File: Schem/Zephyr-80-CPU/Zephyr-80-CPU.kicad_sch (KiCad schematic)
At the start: 0 parts

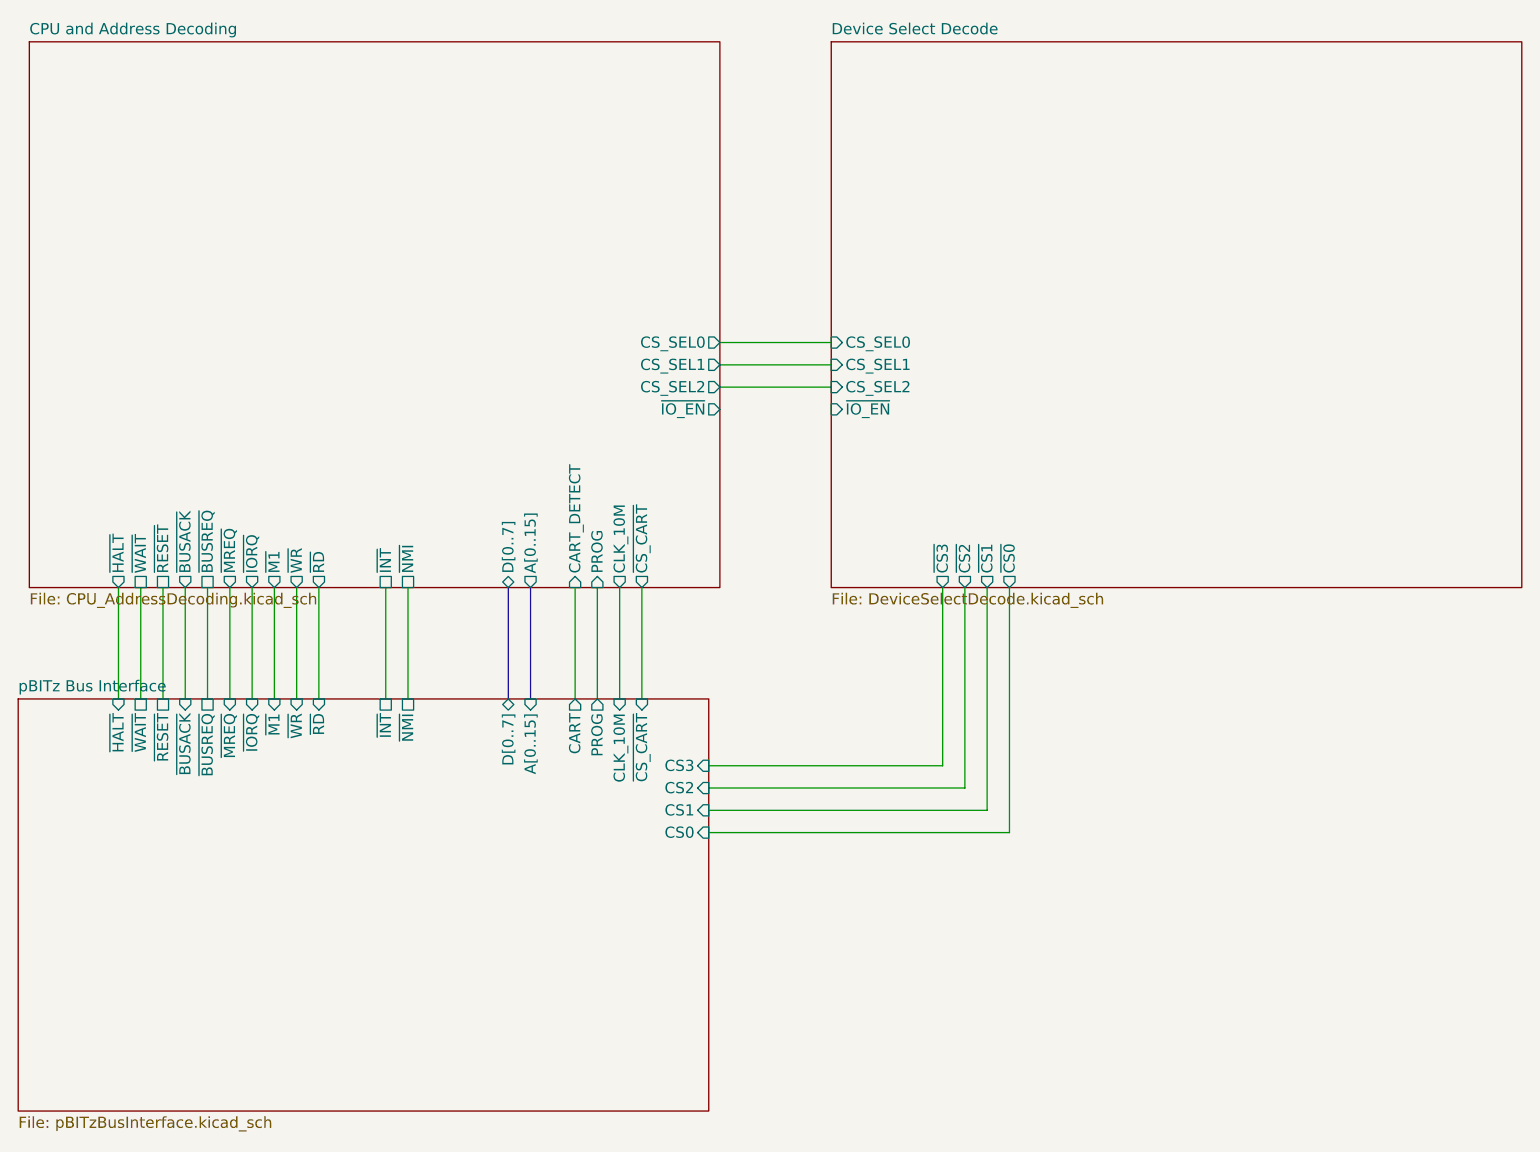
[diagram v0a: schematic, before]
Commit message: Routed the CPU board. Removed the rotary switches decoder
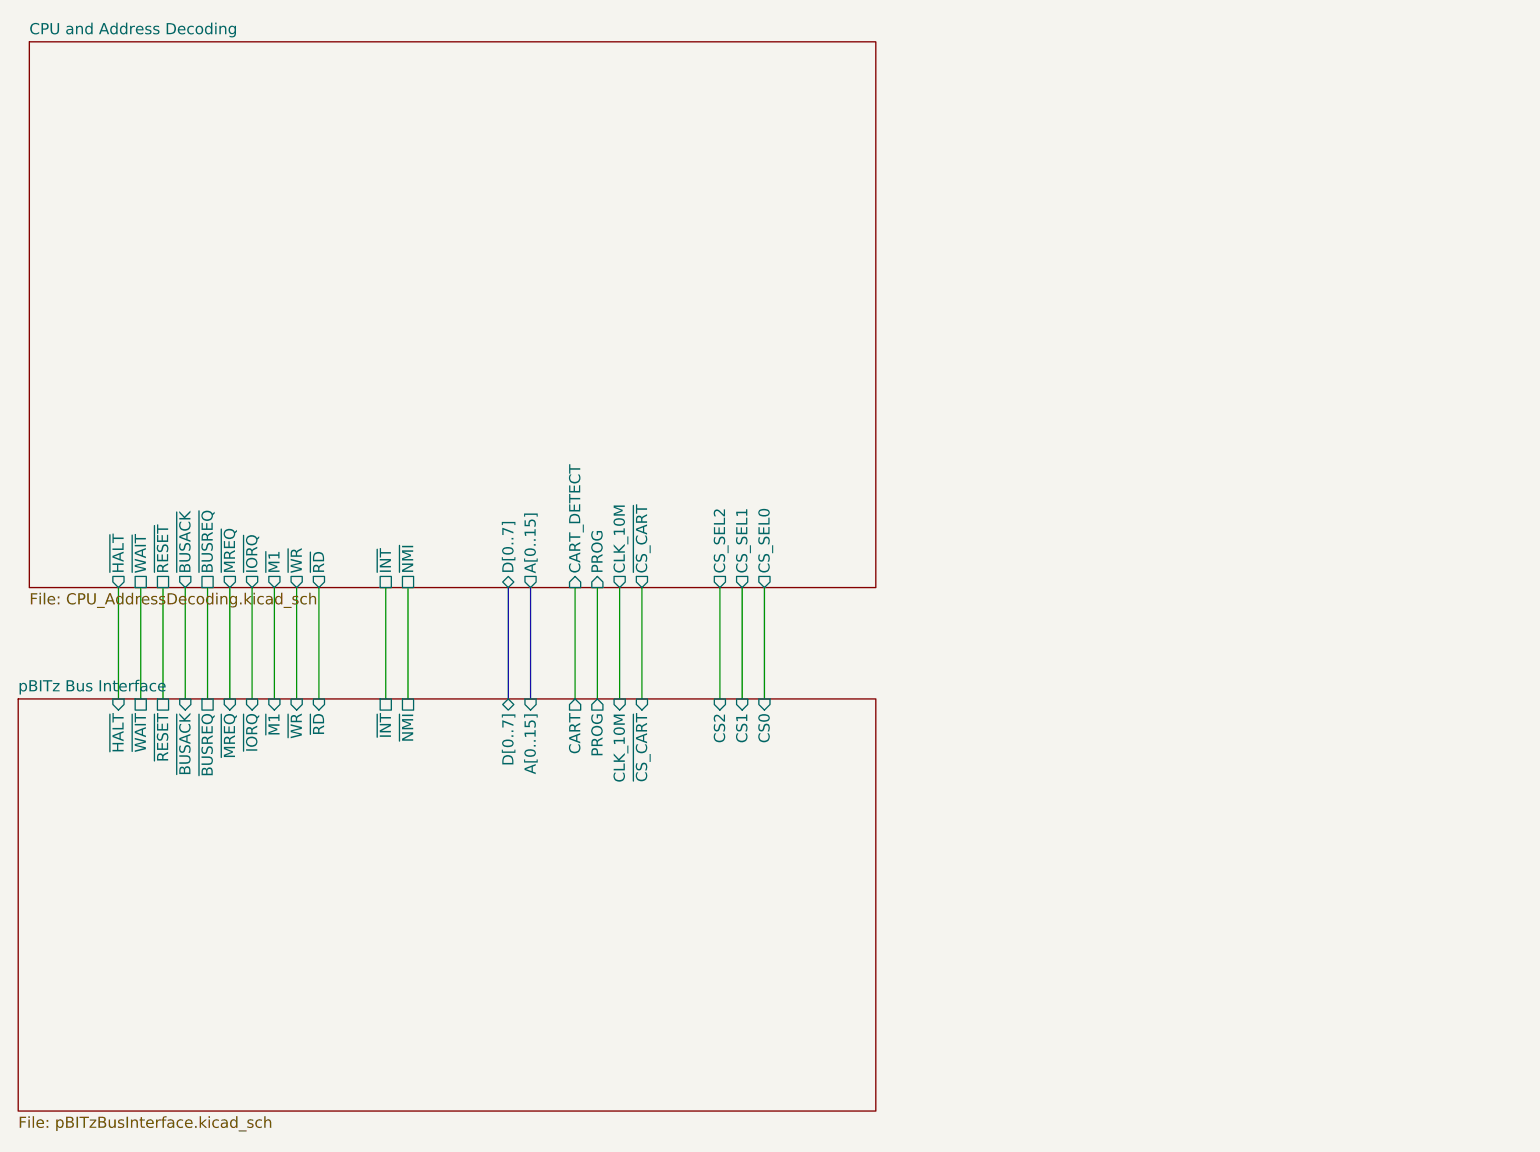
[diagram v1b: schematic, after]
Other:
- removed sheet Device Select Decode
- sheet CPU and Address Decoding ports: added none; removed ~{IO_EN}
- sheet pBITz Bus Interface ports: added none; removed CS3

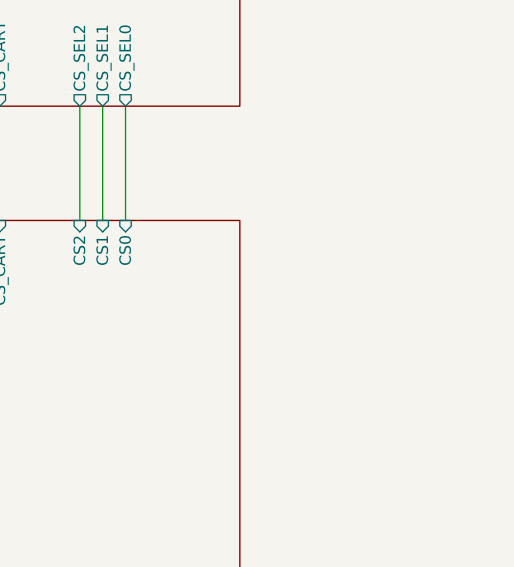
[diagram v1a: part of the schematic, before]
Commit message: Added all the manufacturer part numbers to the KiCad schematics and PCB files. This will make it easier to order the parts for the project and ensure that the correct components are used. I also removed some of the old schematics that were no longer needed, such as the BaudClock, ConsolePort, DeviceSelectDecode, GPIOUserSerial, IO Controller, UserPorts, Video, and Z80HomeBrew schematics. These changes will help to streamline the design and make it easier to understand.
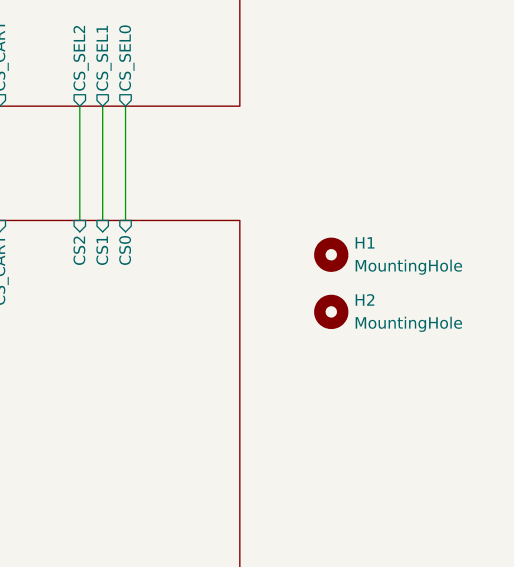
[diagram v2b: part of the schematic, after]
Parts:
- added H1, H2: MountingHole, MountingHole:MountingHole_2.2mm_M2, symbol Mechanical:MountingHole
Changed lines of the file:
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@@
+		)
+	)
+	(symbol
+		(lib_id "Mechanical:MountingHole")
+		(at 134.62 119.38 0)
+		(unit 1)
+		(exclude_from_sim no)
+		(in_bom no)
+		(on_board yes)
+		(dnp no)
+		(fields_autoplaced yes)
+		(property "Reference" "H2"
+			(at 137.16 118.1099 0)
+			(effects
+				(font
+					(size 1.27 1.27)
+				)
+				(justify left)
+			)
+		)
+		(property "Value" "MountingHole"
+			(at 137.16 120.6499 0)
+			(effects
+				(font
+					(size 1.27 1.27)
+				)
+				(justify left)
+			)
+		)
+		(property "Footprint" "MountingHole:MountingHole_2.2mm_M2"
+			(at 134.62 119.38 0)
+			(effects
+				(font
+					(size 1.27 1.27)
+				)
+				(hide yes)
+			)
+		)
+		(property "Datasheet" "~"
+			(at 134.62 119.38 0)
+			(effects
+				(font
+					(size 1.27 1.27)
+				)
+				(hide yes)
+			)
+		)
+		(property "Description" "Mounting Hole without connection"
+			(at 134.62 119.38 0)
+			(effects
+				(font
+					(size 1.27 1.27)
+				)
+				(hide yes)
+			)
+		)
+		(instances
+			(project "Zephyr-80-CPU"
+				(path "/dc6b683c-bfa8-4cb5-a3c8-a89070b5c279"
+					(reference "H2")
+					(unit 1)
+				)
+			)
+		)
+	)
+	(symbol
+		(lib_id "Mechanical:MountingHole")
+		(at 134.62 113.03 0)
+		(unit 1)
+		(exclude_from_sim no)
+		(in_bom no)
+		(on_board yes)
+		(dnp no)
+		(fields_autoplaced yes)
+		(property "Reference" "H1"
+			(at 137.16 111.7599 0)
+			(effects
+				(font
+					(size 1.27 1.27)
+				)
+				(justify left)
+			)
+		)
+		(property "Value" "MountingHole"
+			(at 137.16 114.2999 0)
+			(effects
+				(font
+					(size 1.27 1.27)
+				)
+				(justify left)
+			)
+		)
+		(property "Footprint" "MountingHole:MountingHole_2.2mm_M2"
+			(at 134.62 113.03 0)
+			(effects
+				(font
+					(size 1.27 1.27)
+				)
+				(hide yes)
+			)
+		)
+		(property "Datasheet" "~"
+			(at 134.62 113.03 0)
+			(effects
+				(font
+					(size 1.27 1.27)
+				)
+				(hide yes)
+			)
+		)
+		(property "Description" "Mounting Hole without connection"
+			(at 134.62 113.03 0)
+			(effects
+				(font
+					(size 1.27 1.27)
+				)
+				(hide yes)
+			)
+		)
+		(instances
+			(project ""
+				(path "/dc6b683c-bfa8-4cb5-a3c8-a89070b5c279"
+					(reference "H1")
+					(unit 1)
+				)
+			)
 		)
 	)
